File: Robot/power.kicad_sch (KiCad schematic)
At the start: 28 parts, among them J7 DE9_Receptacle, J8 Battery, J9 Balance, Q1 DMP3036SSD, Q2 Si2003, SW1 Pwr, U2 ICE40UP5K-SG48ITR, U6 NC7SZ175, U7 TLV70212DBVR, U8 TMI6050-33

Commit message: Updated Robot SCH
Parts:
- added R47: 100K, symbol Device:R
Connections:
- net +3.3V: now also R47.2
- net TurnOff: now also R47.1
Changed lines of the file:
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@@
 	)
 	(junction
+		(at 130.81 92.71)
+		(diameter 0)
+		(color 0 0 0 0)
+	)
+	(junction
 		(at 25.4 151.13)
 		(diameter 0)
@@
 	(wire
 		(pts
+			(xy 130.81 92.71) (xy 133.35 92.71)
+		)
+		(stroke
+			(width 0)
+			(type default)
+		)
+	)
+	(wire
+		(pts
 			(xy 138.43 44.45) (xy 138.43 31.75)
 		)
@@
 	(wire
 		(pts
+			(xy 130.81 105.41) (xy 130.81 104.14)
+		)
+		(stroke
+			(width 0)
+			(type default)
+		)
+	)
+	(wire
+		(pts
 			(xy 91.44 161.29) (xy 91.44 163.83)
 		)
@@
 	(wire
 		(pts
-			(xy 129.54 92.71) (xy 133.35 92.71)
+			(xy 129.54 92.71) (xy 130.81 92.71)
 		)
 		(stroke
@@
 	(wire
 		(pts
+			(xy 130.81 92.71) (xy 130.81 96.52)
+		)
+		(stroke
+			(width 0)
+			(type default)
+		)
+	)
+	(wire
+		(pts
 			(xy 45.72 30.48) (xy 69.85 30.48)
 		)
@@
 	)
 	(symbol
+		(lib_id "power:+3.3V")
+		(at 130.81 105.41 180)
+		(unit 1)
+		(exclude_from_sim no)
+		(in_bom yes)
+		(on_board yes)
+		(dnp no)
+		(fields_autoplaced yes)
+		(property "Reference" "#PWR0100"
+			(at 130.81 101.6 0)
+			(effects
+				(font
+					(size 1.27 1.27)
+				)
+				(hide yes)
+			)
+		)
+		(property "Value" "+3.3V"
+			(at 130.81 110.49 0)
+			(effects
+				(font
+					(size 1.27 1.27)
+				)
+			)
+		)
+		(property "Footprint" ""
+			(at 130.81 105.41 0)
+			(effects
+				(font
+					(size 1.27 1.27)
+				)
+				(hide yes)
+			)
+		)
+		(property "Datasheet" ""
+			(at 130.81 105.41 0)
+			(effects
+				(font
+					(size 1.27 1.27)
+				)
+				(hide yes)
+			)
+		)
+		(property "Description" "Power symbol creates a global label with name \"+3.3V\""
+			(at 130.81 105.41 0)
+			(effects
+				(font
+					(size 1.27 1.27)
+				)
+				(hide yes)
+			)
+		)
+		(pin "1"
+		)
+		(instances
+			(project "Robot"
+				(path "/c5aa62e4-5f59-48a4-ae5d-57fc70429dc3/e9eb70e2-5ab4-43f7-8ba2-9f48573f337e"
+					(reference "#PWR0100")
+					(unit 1)
+				)
+			)
+		)
+	)
+	(symbol
 		(lib_id "power:+12V")
 		(at 175.26 24.13 270)
@@
 					(unit 1)
 				)
+			)
+		)
+	)
+	(symbol
+		(lib_id "Device:R")
+		(at 130.81 100.33 0)
+		(unit 1)
+		(exclude_from_sim no)
+		(in_bom yes)
+		(on_board yes)
+		(dnp no)
+		(fields_autoplaced yes)
+		(property "Reference" "R47"
+			(at 133.35 99.0599 0)
+			(effects
+				(font
+					(size 1.27 1.27)
+				)
+				(justify left)
+			)
+		)
+		(property "Value" "100K"
+			(at 133.35 101.5999 0)
+			(effects
+				(font
+					(size 1.27 1.27)
+				)
+				(justify left)
+			)
+		)
+		(property "Footprint" ""
+			(at 129.032 100.33 90)
+			(effects
+				(font
+					(size 1.27 1.27)
+				)
+				(hide yes)
+			)
+		)
+		(property "Datasheet" "~"
+			(at 130.81 100.33 0)
+			(effects
+				(font
+					(size 1.27 1.27)
+				)
+				(hide yes)
+			)
+		)
+		(property "Description" "Resistor"
+			(at 130.81 100.33 0)
+			(effects
+				(font
+					(size 1.27 1.27)
+				)
+				(hide yes)
+			)
+		)
+		(pin "1"
+		)
+		(pin "2"
+		)
+		(instances
+			(project "Robot"
+				(path "/c5aa62e4-5f59-48a4-ae5d-57fc70429dc3/e9eb70e2-5ab4-43f7-8ba2-9f48573f337e"
+					(reference "R47")
+					(unit 1)
+				)

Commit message: Started PCB roughting
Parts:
- J16: renamed from J8; footprint locals:pins4x10 -> locals:TRX
- J17: renamed from J7; footprint easyeda2kicad:DB9-TH_LD09P33E4GV00LF -> easyeda2kicad:DSUB-TH_DMS009PM000XH00
- J18: renamed from J9; footprint Connector_JST:JST_XH_B5B-XH-A_1x05_P2.50mm_Vertical -> Connector_JST:JST_XH_S5B-XH-A-1_1x05_P2.50mm_Horizontal
- Q1: footprint (none) -> easyeda2kicad:SO-8_L4.9-W3.9-P1.27-LS5.9-BL
- R27: renamed from R21; footprint (none) -> Resistor_SMD:R_0603_1608Metric_Pad0.98x0.95mm_HandSolder
- R28: renamed from R22; footprint (none) -> Resistor_SMD:R_0603_1608Metric_Pad0.98x0.95mm_HandSolder
- R29: renamed from R23; footprint (none) -> Resistor_SMD:R_0603_1608Metric_Pad0.98x0.95mm_HandSolder
- R30: renamed from R47; footprint (none) -> Resistor_SMD:R_0603_1608Metric_Pad0.98x0.95mm_HandSolder
- SW2: renamed from SW1; footprint (none) -> locals:KEY-TH_4P-L6.0-W6.0-P4.50-LS6.50
- U7: renamed from U6; footprint (none) -> easyeda2kicad:SC-70-6_L2.0-W1.3-P0.65-LS2.1-BL
- renumbered C25 to C12, C26 to C13, C16 to C14, C11 to C16, C13 to C17, C14 to C18, C11 to C19, C10 to C20, C10 to C21, C12 to C22, C17 to C23, C18 to C24, R17 to R31, U2 to U4, U7 to U8, U8 to U9

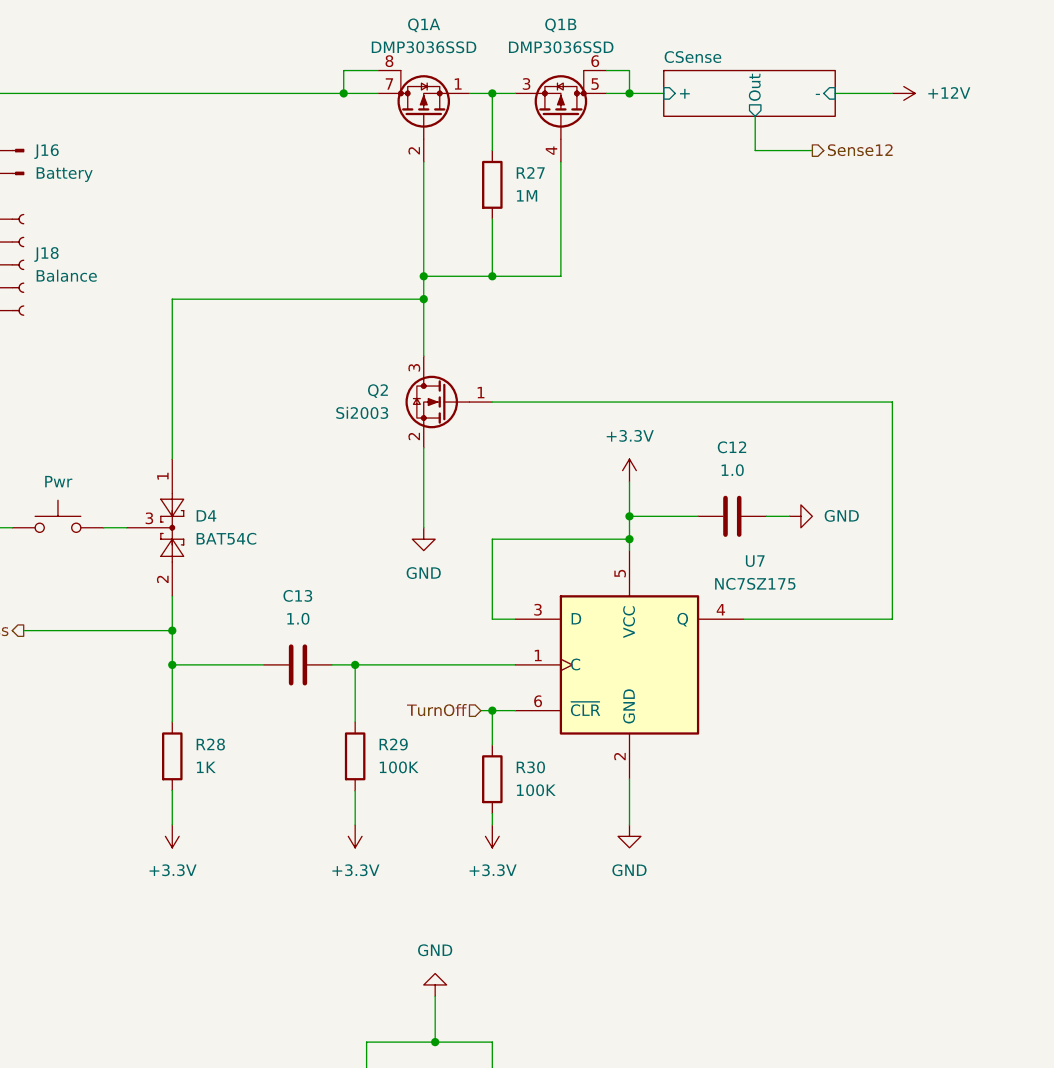
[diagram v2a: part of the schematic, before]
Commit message: Updated SCH & PCB for Robot
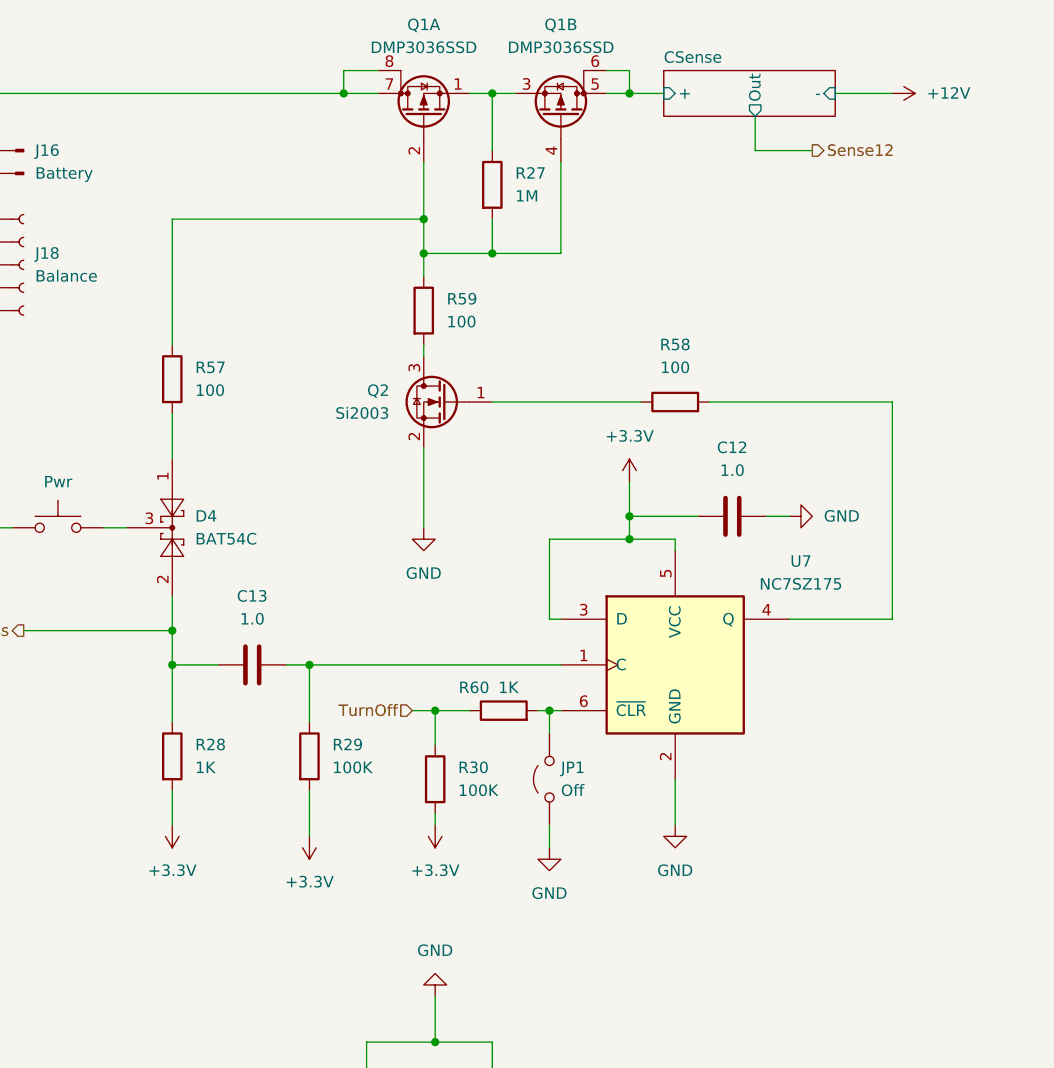
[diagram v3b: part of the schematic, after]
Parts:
- added JP1: Off, Jumper:SolderJumper-2_P1.3mm_Open_Pad1.0x1.5mm, symbol Jumper:Jumper_2_Open
- added R57, R58, R59: 100, Resistor_SMD:R_0603_1608Metric_Pad0.98x0.95mm_HandSolder, symbol Device:R
- added R60: 1K, Resistor_SMD:R_0603_1608Metric_Pad0.98x0.95mm_HandSolder, symbol Device:R
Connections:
- net GND: now also JP1.1 (A)
- net TurnOff: now also R60.1; no longer U7.6 (~{CLR})
- net at Q1.2 (G), Q1.4 (G), R27.2: now also R57.1, R59.1; no longer D4.1, Q2.3 (D)
- net at Q2.1 (G): now also R58.1; no longer U7.4 (Q)
- new net: D4.1, R57.2
- new net: JP1.2 (B), R60.2, U7.6 (~{CLR})
- new net: Q2.3 (D), R59.2
- new net: R58.2, U7.4 (Q)
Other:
- moved on the sheet: C13, R29, R30, U7

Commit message: Updated PCB & Patterns for Robot
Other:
- company: (none) -> RoboWay
- title: (none) -> Power
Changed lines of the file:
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@@
 	(generator_version "9.0")
 	(paper "A4")
+	(title_block
+		(title "Power")
+		(company "RoboWay")
+	)
 	(junction
 		(at 116.84 148.59)

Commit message: Updated PCB for Robot
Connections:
- net CSense/+: now also Q1.7 (D), Q1.8 (D); no longer Q1.5 (D), Q1.6 (D)
- net GND: now also J16.2 (Pin_2); no longer J16.1 (Pin_1)
- net PwrBtnPress: now also D4.1; no longer D4.2
- net at R57.2: now also D4.2; no longer D4.1
- net at R27.2, R57.1, R59.1: now also Q1.2 (G), Q1.4 (G); no longer Q1.2 (G), Q1.4 (G)
- new net: J16.1 (Pin_1), J17.1, J17.6, Q1.5 (D), Q1.6 (D)
- new net: Q1.1 (S), Q1.3 (S), R27.1
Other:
- moved on the sheet: J16
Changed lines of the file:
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@@
 		(lib_id "Diode:BAT54C")
 		(at 95.25 72.39 270)
-		(unit 1)
-		(exclude_from_sim no)
-		(in_bom yes)
-		(on_board yes)
-		(dnp no)
-		(fields_autoplaced yes)
+		(mirror x)
+		(unit 1)
+		(exclude_from_sim no)
+		(in_bom yes)
+		(on_board yes)
+		(dnp no)
 		(property "Reference" "D4"
 			(at 97.79 71.1199 90)
@@
 		)
 		(property "Footprint" "Package_TO_SOT_SMD:SOT-23"
-			(at 98.425 74.295 0)
+			(at 98.425 70.485 0)
 			(effects
 				(font
@@
 		)
 		(property "Datasheet" "http://www.diodes.com/_files/datasheets/ds11005.pdf"
-			(at 95.25 70.358 0)
+			(at 95.25 74.422 0)
 			(effects
 				(font
@@
 	(symbol
 		(lib_id "Connector:Conn_01x02_Pin")
-		(at 78.74 33.02 180)
-		(unit 1)
-		(exclude_from_sim no)
-		(in_bom yes)
-		(on_board yes)
-		(dnp no)
-		(fields_autoplaced yes)
+		(at 78.74 30.48 0)
+		(mirror y)
+		(unit 1)
+		(exclude_from_sim no)
+		(in_bom yes)
+		(on_board yes)
+		(dnp no)
 		(property "Reference" "J16"
-			(at 80.01 30.4799 0)
-			(effects
-				(font
-					(size 1.27 1.27)
-				)
-				(justify right)
+			(at 78.105 25.4 0)
+			(effects
+				(font
+					(size 1.27 1.27)
+				)
 			)
 		)
 		(property "Value" "Battery"
-			(at 80.01 33.0199 0)
-			(effects
-				(font
-					(size 1.27 1.27)
-				)
-				(justify right)
+			(at 78.105 27.94 0)
+			(effects
+				(font
+					(size 1.27 1.27)
+				)
 			)
 		)
 		(property "Footprint" "locals:TRX"
-			(at 78.74 33.02 0)
+			(at 78.74 30.48 0)
 			(effects
 				(font
@@
 		)
 		(property "Datasheet" "~"
-			(at 78.74 33.02 0)
+			(at 78.74 30.48 0)
 			(effects
 				(font
@@
 		)
 		(property "Description" "Generic connector, single row, 01x02, script generated"
-			(at 78.74 33.02 0)
+			(at 78.74 30.48 0)
 			(effects
 				(font
@@
 		(at 138.43 26.67 270)
 		(mirror x)
-		(unit 2)
+		(unit 1)
 		(exclude_from_sim no)
 		(in_bom yes)
@@
 				(path "/c5aa62e4-5f59-48a4-ae5d-57fc70429dc3/e9eb70e2-5ab4-43f7-8ba2-9f48573f337e"
 					(reference "Q1")
-					(unit 2)
+					(unit 1)
 				)
 			)
@@
 		(lib_id "Transistor_FET:Q_Dual_PMOS_S1G1S2G2D2D2D1D1")
 		(at 123.19 26.67 90)
-		(unit 1)
+		(unit 2)
 		(exclude_from_sim no)
 		(in_bom yes)
@@
 				(path "/c5aa62e4-5f59-48a4-ae5d-57fc70429dc3/e9eb70e2-5ab4-43f7-8ba2-9f48573f337e"
 					(reference "Q1")
-					(unit 1)
-				)
-			)
+					(unit 2)
+				)
+			)

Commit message: Updated PCB for Robot (routing in progress)
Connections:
- net +3.3V is gone; now on net +3V3: C12.1, R28.2, R29.2, R30.2, U7.3 (D), U7.5 (VCC)

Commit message: Added LCSC PN for all PCBA components
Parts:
- U4: MPN (none) -> C2678152
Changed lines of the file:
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@@
+			)
+		)
+		(property "MPN" "C2678152"
+			(at 147.32 151.13 0)
+			(effects
+				(font
+					(size 1.27 1.27)
+				)
+				(hide yes)
 			)
 		)
